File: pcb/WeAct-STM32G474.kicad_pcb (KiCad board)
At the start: 2 copper layers, 50 x 40 mm, 38 parts, among them J1 P1, J2 P2, U1 AMS1117-3.3, U2 STM32G474CBTx, U3 SRV05-4, Y1 X_24MHZ

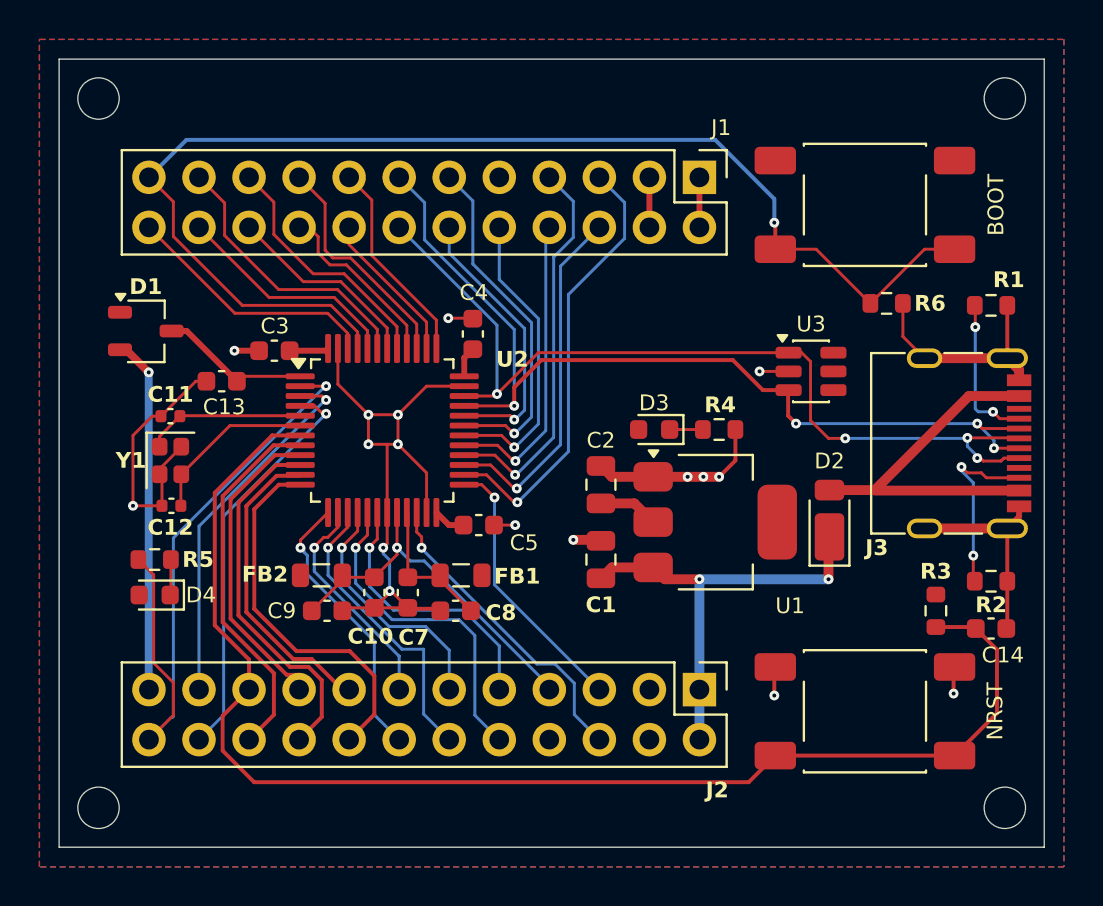
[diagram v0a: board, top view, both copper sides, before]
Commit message: fix usb type-c placement
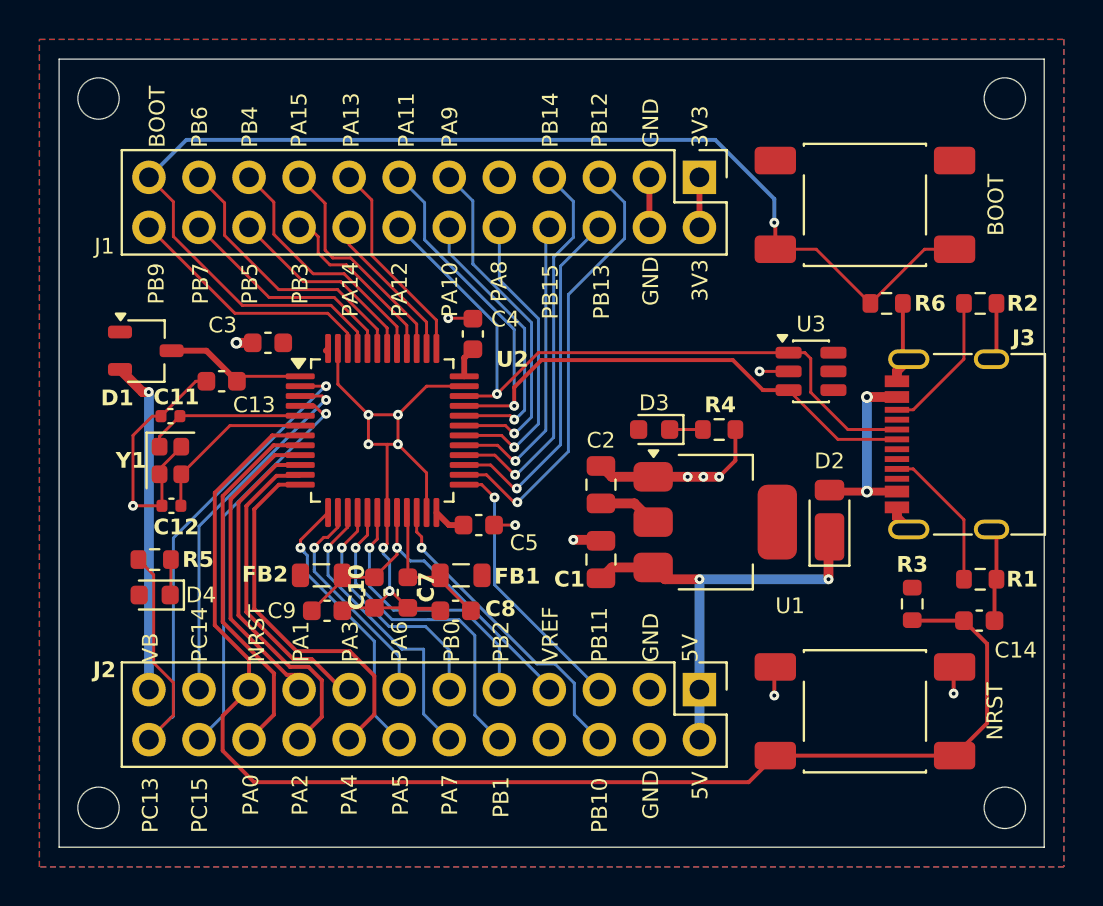
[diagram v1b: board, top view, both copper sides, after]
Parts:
- moved R2 14.1 mm to (165.8, 90.4)
- moved R1 13.9 mm to (165.8, 104.4)
- moved J3 1.25 mm to (165.2, 97.5), turned to 90 degrees
- moved R3 1.25 mm to (162.3, 105.7)
- moved D1 1.00 mm to (123.4, 92.8)
- moved C14 0.72 mm to (165.7, 106.5)
- moved C3 0.52 mm to (129.6, 92.4)
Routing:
- net PA12: track 46.6 -> 36.0 mm, vias 4 -> 1
- net VBUS: track 19.9 -> 10.2 mm, vias 0 -> 2
- net PA11: track 48.8 -> 39.2 mm, vias 4 -> 1
- net GND: track 89.7 -> 80.5 mm
- net Net-(J3-CC2): track 9.23 -> 7.29 mm, vias 2 -> 0
- net +3V3: track 10.8 -> 8.94 mm
- net VB: track 18.0 -> 17.1 mm
- net NRST: track 68.1 -> 68.9 mm
- net Net-(J3-CC1): track 7.69 -> 7.49 mm, vias 2 -> 0
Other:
- board text added: "3V3"
- board text added: "5V"
- board text added: "BOOT"
- board text added: "GND"
- board text added: "NRST"
- board text added: "PA0"
- board text added: "PA1"
- board text added: "PA10"
- board text added: "PA11"
- board text added: "PA12"
- board text added: "PA13"
- board text added: "PA14"
- board text added: "PA15"
- board text added: "PA2"
- board text added: "PA3"
- board text added: "PA4"
- board text added: "PA5"
- board text added: "PA6"
- board text added: "PA7"
- board text added: "PA8"
- board text added: "PA9"
- board text added: "PB0"
- board text added: "PB1"
- board text added: "PB10"
- board text added: "PB11"
- board text added: "PB12"
- board text added: "PB13"
- board text added: "PB14"
- board text added: "PB15"
- board text added: "PB2"
- board text added: "PB3"
- board text added: "PB4"
- board text added: "PB5"
- board text added: "PB6"
- board text added: "PB7"
- board text added: "PB9"
- board text added: "PC13"
- board text added: "PC14"
- board text added: "PC15"
- board text added: "VB"
- board text added: "VREF"

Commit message: update new
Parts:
- C11, C12: value C_10PF_0402 -> C_10PF_0603; footprint Capacitor_SMD:C_0402_1005Metric -> Capacitor_SMD:C_0603_1608Metric
- renumbered NRST to NRST1
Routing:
- net GND: track 80.5 -> 77.8 mm
